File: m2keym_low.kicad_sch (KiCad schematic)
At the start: 14 parts, among them J5 Bus_M.2_1-2199230-6

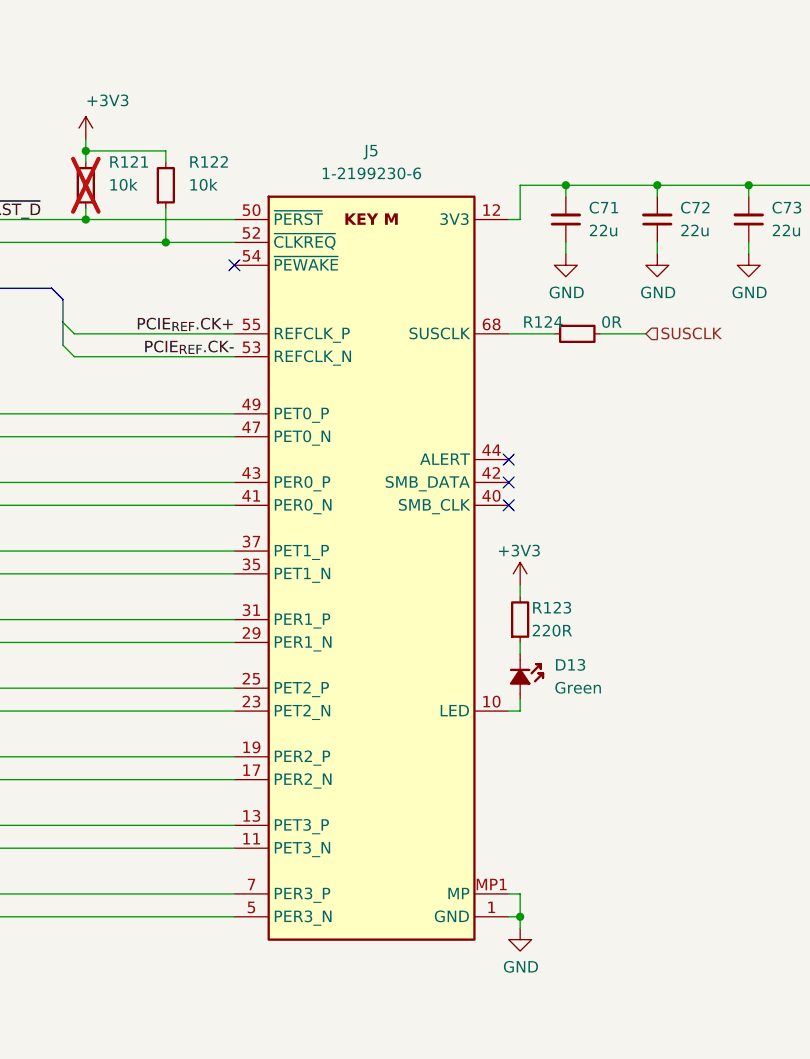
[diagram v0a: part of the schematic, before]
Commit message: [#65446] Update the M.2 connector from the library
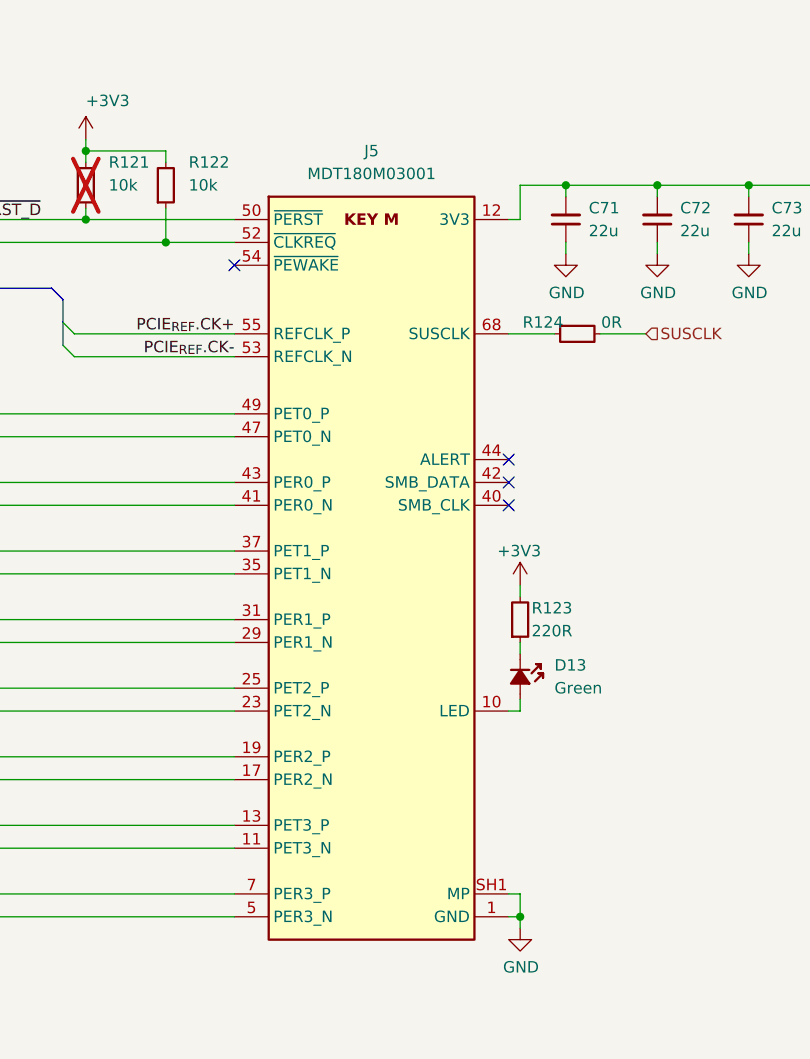
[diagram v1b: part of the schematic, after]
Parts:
- J5: value Bus_M.2_1-2199230-6 -> Bus_M.2_MDT180M03001; MPN 1-2199230-6 -> MDT180M03001; Manufacturer TE Connectivity -> Amphenol
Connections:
- net GND: now also J5.SH1 (MP), J5.SH2 (MP); no longer J5.MP1 (MP), J5.MP2 (MP)
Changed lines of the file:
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@@
       (effects (font (size 1.27 1.27) (thickness 0.15)))
     )
-    (property "Value" "Bus_M.2_1-2199230-6" (at 246.38 96.52 0)
+    (property "Value" "Bus_M.2_MDT180M03001" (at 246.38 96.52 0)
       (effects (font (size 1.27 1.27) (thickness 0.15)) (justify left bottom) hide)
     )
@@
       (effects (font (size 1.27 1.27) (thickness 0.15)) (justify left bottom) hide)
     )
-    (property "Datasheet" "https://www.te.com/commerce/DocumentDelivery/DDEController?Action=srchrtrv&DocNm=2199230&DocType=Customer+Drawing&DocLang=English" (at 246.38 101.6 0)
+    (property "Datasheet" "https://cdn.amphenol-cs.com/media/wysiwyg/files/drawing/mdt180xxx001.pdf" (at 246.38 101.6 0)
       (effects (font (size 1.27 1.27) (thickness 0.15)) (justify left bottom) hide)
     )
-    (property "Manufacturer" "TE Connectivity" (at 246.38 104.14 0)
+    (property "Manufacturer" "Amphenol" (at 246.38 104.14 0)
       (effects (font (size 1.27 1.27) (thickness 0.15)) (justify left bottom) hide)
     )
-    (property "MPN" "1-2199230-6" (at 215.9 83.82 0)
+    (property "MPN" "MDT180M03001" (at 215.9 83.82 0)
       (effects (font (size 1.27 1.27) (thickness 0.15)))
     )
@@
     (pin "17")
     (pin "27")
-    (pin "MP1")
+    (pin "SH2")
     (pin "19")
     (pin "25")
@@
     (pin "70")
     (pin "31")
-    (pin "MP2")
+    (pin "SH1")
     (pin "11")
     (pin "14")

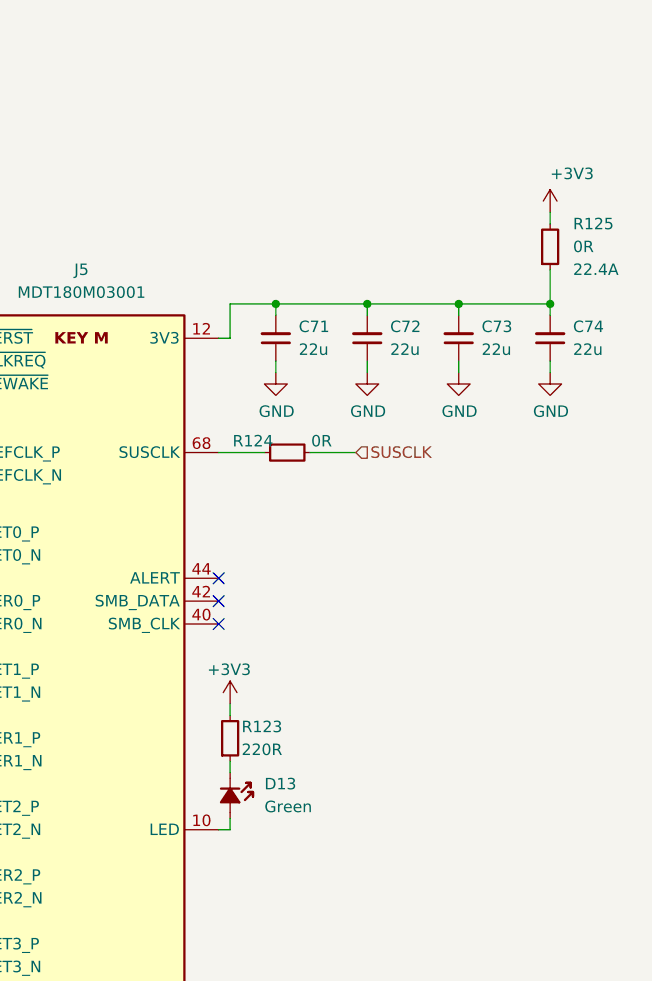
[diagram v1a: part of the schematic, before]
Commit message: [#65447] Fix rotated LEDs, overlapping text and symbols, add rules
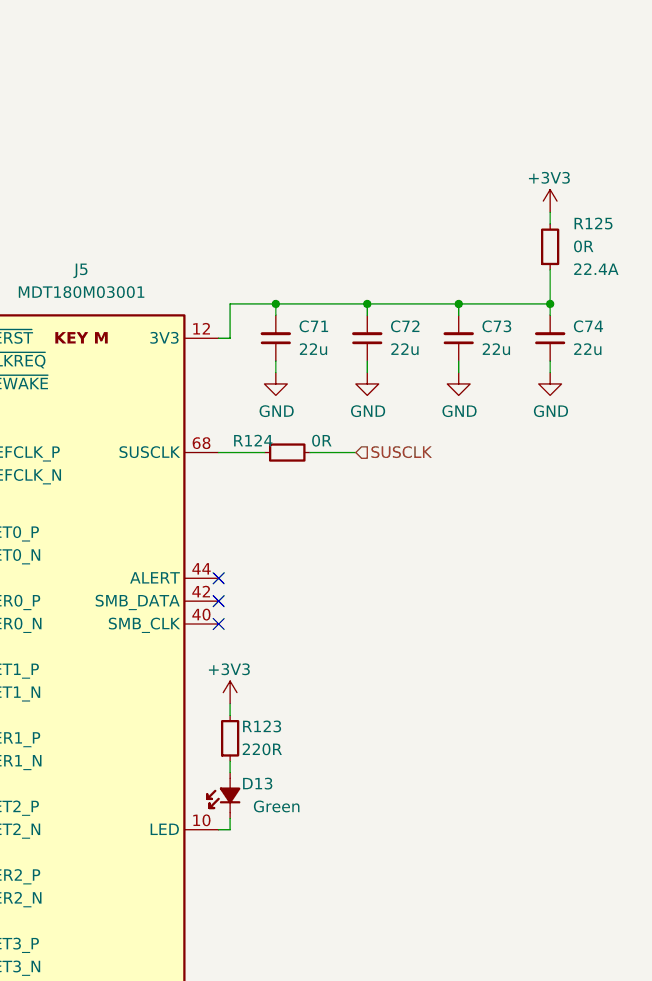
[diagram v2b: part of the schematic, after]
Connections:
- net at R123.1: now also D13.2 (A); no longer D13.1 (C)
- net at J5.10 (LED): now also D13.1 (C); no longer D13.2 (A)
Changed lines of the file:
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@@
   )
   (symbol (lib_id "antmicropower:+3V3") (at 267.97 74.93 0) (unit 1)
-    (in_bom yes) (on_board yes) (dnp no) (fields_autoplaced)
+    (in_bom yes) (on_board yes) (dnp no)
     (property "Reference" "#PWR0163" (at 267.97 78.74 0)
       (effects (font (size 1.27 1.27)) (justify left bottom) hide)
     )
-    (property "Value" "+3V3" (at 267.97 71.374 0)
-      (effects (font (size 1.27 1.27)) (justify left bottom))
+    (property "Value" "+3V3" (at 265.43 71.12 0)
+      (effects (font (size 1.27 1.27)) (justify left))
     )
     (property "Footprint" "" (at 267.97 74.93 0)
@@
         (path "/1b8c34da-dad5-4b0b-8c4b-45db766c4dfa/2acc1b08-bc1c-4714-8c61-ebdd69dbc5a5"
           (reference "#PWR0156") (unit 1)
+        )
+      )
+    )
+  )
+  (symbol (lib_id "antmicroLEDIndicationDiscrete:LED_G_0603_LTST-C190GKT") (at 232.41 142.24 90) (unit 1)
+    (in_bom yes) (on_board yes) (dnp no)
+    (property "Reference" "D13" (at 233.68 138.43 90)
+      (effects (font (size 1.27 1.27)) (justify right))
+    )
+    (property "Value" "LED_G_0603_LTST-C190GKT" (at 228.6 139.7 0)
+      (effects (font (size 1.27 1.27) (thickness 0.15)) (justify left bottom) hide)
+    )
+    (property "Footprint" "antmicro-footprints:LED_0603_1608Metric_G" (at 242.57 119.38 0)
+      (effects (font (size 1.27 1.27) (thickness 0.15)) (justify left bottom) hide)
+    )
+    (property "Datasheet" "https://media.digikey.com/pdf/Data%20Sheets/Lite-On%20PDFs/LTST-C190GKT.pdf" (at 245.11 119.38 0)
+      (effects (font (size 1.27 1.27) (thickness 0.15)) (justify left bottom) hide)
+    )
+    (property "MPN" "LTST-C190GKT" (at 229.235 136.525 90)
+      (effects (font (size 1.27 1.27) (thickness 0.15)) (justify left bottom) hide)
+    )
+    (property "Manufacturer" "Lite-On" (at 250.19 119.38 0)
+      (effects (font (size 1.27 1.27) (thickness 0.15)) (justify left bottom) hide)
+    )
+    (property "Author" "Antmicro" (at 252.73 119.38 0)
+      (effects (font (size 1.27 1.27) (thickness 0.15)) (justify left bottom) hide)
+    )
+    (property "License" "Apache-2.0" (at 255.27 119.38 0)
+      (effects (font (size 1.27 1.27) (thickness 0.15)) (justify left bottom) hide)
+    )
+    (property "Public" "False" (at 250.19 121.92 0)
+      (effects (font (size 1.27 1.27)) (justify left bottom) hide)
+    )
+    (property "Color" "Green" (at 234.95 140.97 90)
+      (effects (font (size 1.27 1.27)) (justify right))
+    )
+    (pin "1")
+    (pin "2")
+    (instances
+      (project "com-express-7-baseboard"
+        (path "/1b8c34da-dad5-4b0b-8c4b-45db766c4dfa/2acc1b08-bc1c-4714-8c61-ebdd69dbc5a5"
+          (reference "D13") (unit 1)
         )
       )
@@
         )
       )
-    )
-  )
-  (symbol (lib_id "antmicroLEDIndicationDiscrete:LED_G_0603_LTST-C190GKT") (at 232.41 137.16 270) (unit 1)
-    (in_bom yes) (on_board yes) (dnp no) (fields_autoplaced)
-    (property "Reference" "D13" (at 236.22 138.43 90)
-      (effects (font (size 1.27 1.27)) (justify left))
-    )
-    (property "Value" "LED_G_0603_LTST-C190GKT" (at 236.22 139.7 0)
-      (effects (font (size 1.27 1.27) (thickness 0.15)) (justify left bottom) hide)
-    )
-    (property "Footprint" "antmicro-footprints:LED_0603_1608Metric_G" (at 222.25 160.02 0)
-      (effects (font (size 1.27 1.27) (thickness 0.15)) (justify left bottom) hide)
-    )
-    (property "Datasheet" "https://media.digikey.com/pdf/Data%20Sheets/Lite-On%20PDFs/LTST-C190GKT.pdf" (at 219.71 160.02 0)
-      (effects (font (size 1.27 1.27) (thickness 0.15)) (justify left bottom) hide)
-    )
-    (property "MPN" "LTST-C190GKT" (at 235.585 142.875 90)
-      (effects (font (size 1.27 1.27) (thickness 0.15)) (justify left bottom) hide)
-    )
-    (property "Manufacturer" "Lite-On" (at 214.63 160.02 0)
-      (effects (font (size 1.27 1.27) (thickness 0.15)) (justify left bottom) hide)
-    )
-    (property "Author" "Antmicro" (at 212.09 160.02 0)
-      (effects (font (size 1.27 1.27) (thickness 0.15)) (justify left bottom) hide)
-    )
-    (property "License" "Apache-2.0" (at 209.55 160.02 0)
-      (effects (font (size 1.27 1.27) (thickness 0.15)) (justify left bottom) hide)
-    )
-    (property "Public" "False" (at 214.63 157.48 0)
-      (effects (font (size 1.27 1.27)) (justify left bottom) hide)
-    )
-    (property "Color" "Green" (at 236.22 140.97 90)
-      (effects (font (size 1.27 1.27)) (justify left))
-    )
-    (pin "1")
-    (pin "2")
-    (instances
-      (project "com-express-7-baseboard"
-        (path "/1b8c34da-dad5-4b0b-8c4b-45db766c4dfa/2acc1b08-bc1c-4714-8c61-ebdd69dbc5a5"
-          (reference "D13") (unit 1)
-        )
-      )

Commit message: [#65840] Roughly route PCIe, GbE
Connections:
- net M2_3V3: now reaches C71.2, C72.2, C73.2, C74.2, J5.12 (3V3), J5.14 (3V3), J5.16 (3V3), J5.18 (3V3), J5.2 (3V3), J5.4 (3V3), J5.70 (3V3), J5.72 (3V3), J5.74 (3V3), R125.1
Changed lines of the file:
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@@
+    (effects (font (size 1.27 1.27)) (justify left bottom))
+  )
+  (label "M2_3V3" (at 232.41 85.09 0) (fields_autoplaced)
     (effects (font (size 1.27 1.27)) (justify left bottom))
   )
@@
   (symbol (lib_id "antmicroResistors0402:R_0R_0402") (at 236.22 101.6 0) (unit 1)
     (in_bom yes) (on_board yes) (dnp no)
-    (property "Reference" "R124" (at 234.95 100.33 0)
-      (effects (font (size 1.27 1.27) (thickness 0.15)))
-    )
+    (property "Reference" "R124" (at 233.68 100.33 0)
+      (effects (font (size 1.27 1.27) (thickness 0.15)))
+    )

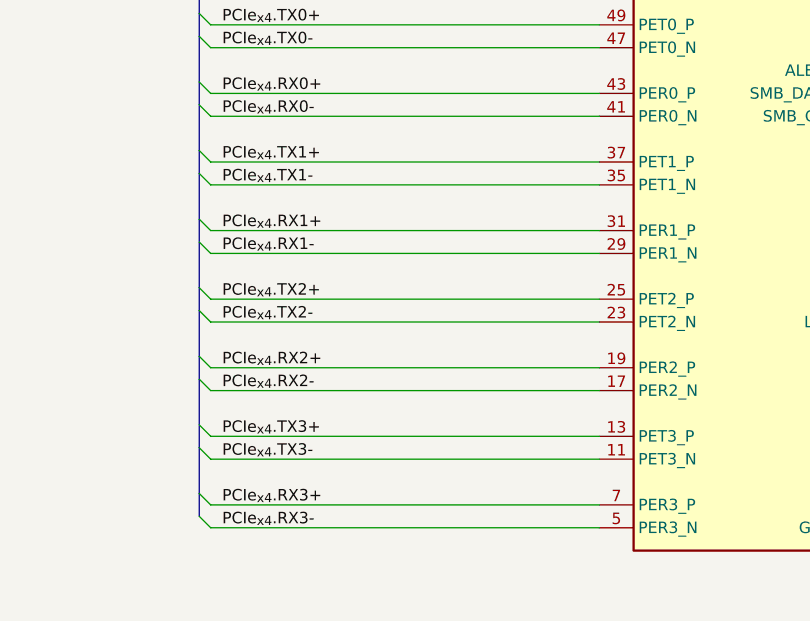
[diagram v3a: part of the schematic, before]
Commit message: [#65840] Route PCIe clock fanout, improve PCIe lines layout
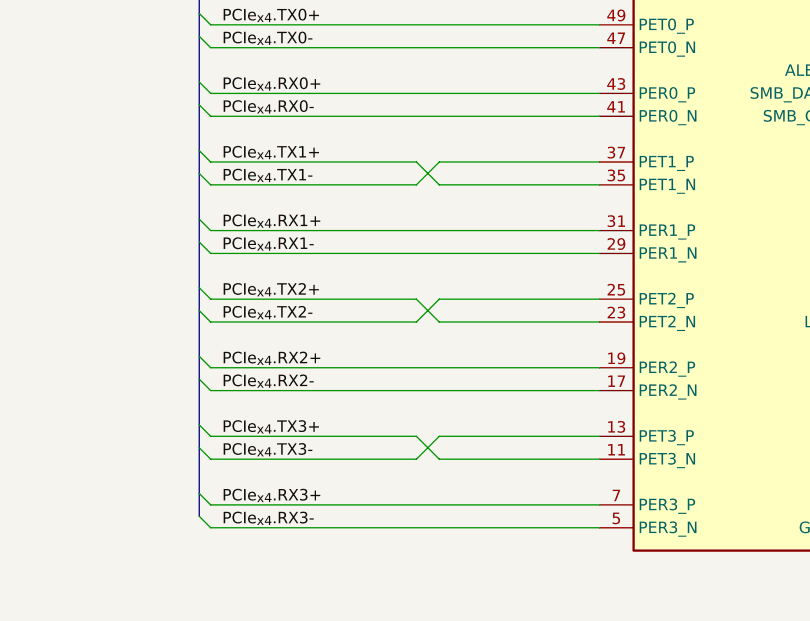
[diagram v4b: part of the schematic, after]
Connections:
- net PCIe_{x4}.TX1+: now also J5.35 (PET1_N); no longer J5.37 (PET1_P)
- net PCIe_{x4}.TX1-: now also J5.37 (PET1_P); no longer J5.35 (PET1_N)
- net PCIe_{x4}.TX2+: now also J5.23 (PET2_N); no longer J5.25 (PET2_P)
- net PCIe_{x4}.TX2-: now also J5.25 (PET2_P); no longer J5.23 (PET2_N)
- net PCIe_{x4}.TX3+: now also J5.11 (PET3_N); no longer J5.13 (PET3_P)
- net PCIe_{x4}.TX3-: now also J5.13 (PET3_P); no longer J5.11 (PET3_N)
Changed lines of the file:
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@@
+    (stroke (width 0) (type default))
+  )
+  (wire (pts (xy 200.66 156.21) (xy 182.88 156.21))
     (stroke (width 0) (type default))
   )
@@
     (stroke (width 0) (type default))
   )
+  (wire (pts (xy 157.48 125.73) (xy 180.34 125.73))
+    (stroke (width 0) (type default))
+  )
   (bus (pts (xy 156.21 132.08) (xy 156.21 134.62))
     (stroke (width 0) (type default))
   )
-  (wire (pts (xy 157.48 140.97) (xy 200.66 140.97))
-    (stroke (width 0) (type default))
-  )
   (wire (pts (xy 200.66 104.14) (xy 182.88 104.14))
     (stroke (width 0) (type default))
@@
     (stroke (width 0) (type default))
   )
+  (wire (pts (xy 182.88 128.27) (xy 200.66 128.27))
+    (stroke (width 0) (type default))
+  )
   (wire (pts (xy 200.66 120.65) (xy 157.48 120.65))
     (stroke (width 0) (type default))
@@
     (stroke (width 0) (type default))
   )
-  (wire (pts (xy 157.48 125.73) (xy 200.66 125.73))
-    (stroke (width 0) (type default))
-  )
   (wire (pts (xy 157.48 113.03) (xy 200.66 113.03))
     (stroke (width 0) (type default))
@@
     (stroke (width 0) (type default))
   )
-  (wire (pts (xy 157.48 128.27) (xy 200.66 128.27))
+  (wire (pts (xy 182.88 143.51) (xy 200.66 143.51))
     (stroke (width 0) (type default))
   )
@@
     (stroke (width 0) (type default))
   )
+  (wire (pts (xy 182.88 125.73) (xy 180.34 128.27))
+    (stroke (width 0) (type default))
+  )
+  (wire (pts (xy 157.48 143.51) (xy 180.34 143.51))
+    (stroke (width 0) (type default))
+  )
   (wire (pts (xy 193.04 81.28) (xy 184.15 81.28))
     (stroke (width 0) (type default))
@@
     (stroke (width 0) (type default))
   )
-  (wire (pts (xy 157.48 143.51) (xy 200.66 143.51))
-    (stroke (width 0) (type default))
-  )
   (wire (pts (xy 184.15 81.28) (xy 184.15 82.55))
     (stroke (width 0) (type default))
@@
     (stroke (width 0) (type default))
   )
+  (wire (pts (xy 200.66 140.97) (xy 182.88 140.97))
+    (stroke (width 0) (type default))
+  )
   (wire (pts (xy 237.49 92.71) (xy 237.49 91.44))
     (stroke (width 0) (type default))
   )
+  (wire (pts (xy 157.48 140.97) (xy 180.34 140.97))
+    (stroke (width 0) (type default))
+  )
   (wire (pts (xy 149.86 91.44) (xy 193.04 91.44))
     (stroke (width 0) (type default))
   )
+  (wire (pts (xy 157.48 156.21) (xy 180.34 156.21))
+    (stroke (width 0) (type default))
+  )
   (bus (pts (xy 156.21 134.62) (xy 156.21 139.7))
     (stroke (width 0) (type default))
@@
     (stroke (width 0) (type default))
   )
+  (wire (pts (xy 182.88 140.97) (xy 180.34 143.51))
+    (stroke (width 0) (type default))
+  )
   (wire (pts (xy 184.15 88.9) (xy 200.66 88.9))
     (stroke (width 0) (type default))
   )
+  (wire (pts (xy 180.34 140.97) (xy 182.88 143.51))
+    (stroke (width 0) (type default))
+  )
   (wire (pts (xy 200.66 133.35) (xy 157.48 133.35))
     (stroke (width 0) (type default))
@@
     (stroke (width 0) (type default))
   )
-  (wire (pts (xy 157.48 156.21) (xy 200.66 156.21))
-    (stroke (width 0) (type default))
-  )
-  (wire (pts (xy 157.48 158.75) (xy 200.66 158.75))
-    (stroke (width 0) (type default))
-  )
   (bus (pts (xy 156.21 149.86) (xy 156.21 154.94))
     (stroke (width 0) (type default))
   )
+  (wire (pts (xy 182.88 158.75) (xy 200.66 158.75))
+    (stroke (width 0) (type default))
+  )
   (bus (pts (xy 156.21 127) (xy 156.21 132.08))
     (stroke (width 0) (type default))
@@
     (stroke (width 0) (type default))
   )
+  (wire (pts (xy 200.66 125.73) (xy 182.88 125.73))
+    (stroke (width 0) (type default))
+  )
   (bus (pts (xy 156.21 111.76) (xy 156.21 116.84))
     (stroke (width 0) (type default))
   )
+  (wire (pts (xy 180.34 156.21) (xy 182.88 158.75))
+    (stroke (width 0) (type default))
+  )
   (wire (pts (xy 231.14 143.51) (xy 232.41 143.51))
     (stroke (width 0) (type default))
@@
     (stroke (width 0) (type default))
   )
+  (wire (pts (xy 180.34 125.73) (xy 182.88 128.27))
+    (stroke (width 0) (type default))
+  )
   (bus (pts (xy 156.21 162.56) (xy 156.21 165.1))
     (stroke (width 0) (type default))
   )
+  (wire (pts (xy 157.48 128.27) (xy 180.34 128.27))
+    (stroke (width 0) (type default))
+  )
   (wire (pts (xy 232.41 142.24) (xy 232.41 143.51))
     (stroke (width 0) (type default))
@@
     (stroke (width 0) (type default))
   )
+  (wire (pts (xy 182.88 156.21) (xy 180.34 158.75))
+    (stroke (width 0) (type default))
+  )
   (bus (pts (xy 181.61 97.79) (xy 180.34 96.52))
     (stroke (width 0) (type default))
   )
+  (wire (pts (xy 157.48 158.75) (xy 180.34 158.75))
+    (stroke (width 0) (type default))
+  )
